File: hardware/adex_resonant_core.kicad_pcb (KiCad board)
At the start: 4 copper layers, 70 x 70 mm, 286 parts

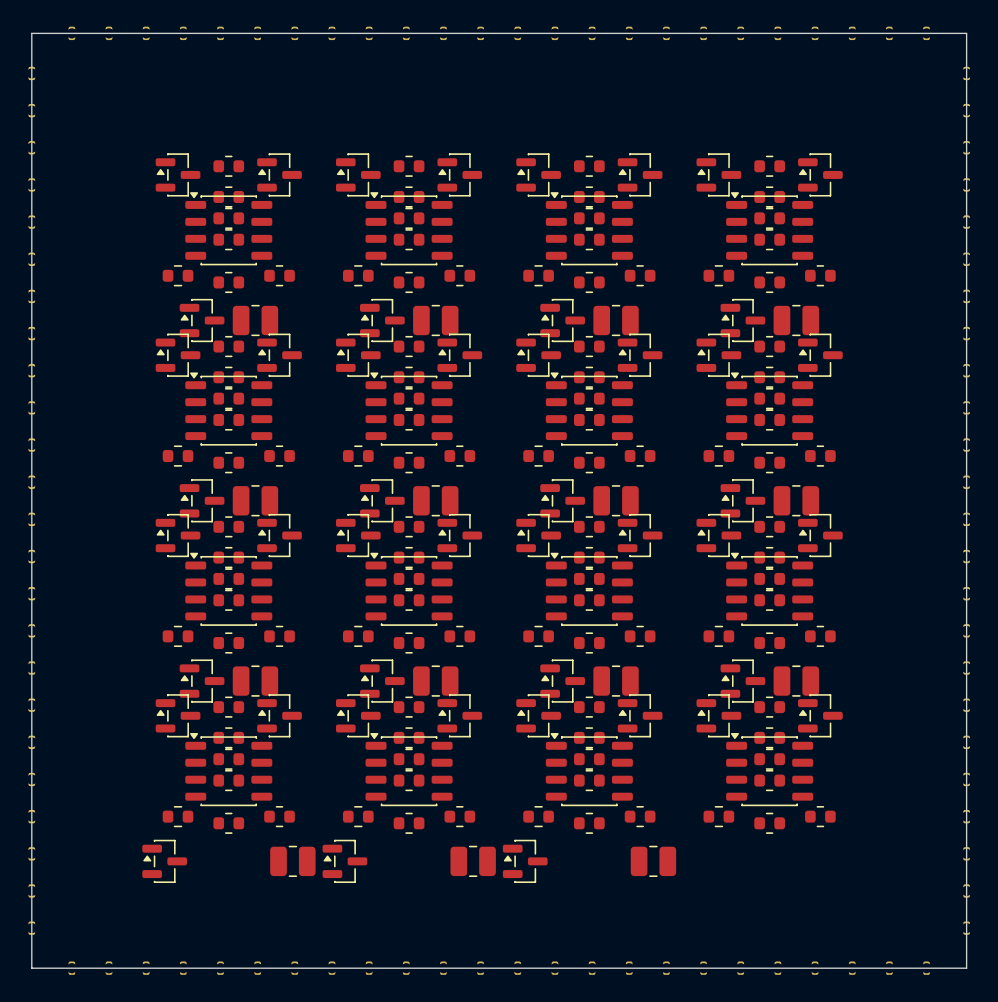
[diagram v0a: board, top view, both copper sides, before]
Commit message: fix(hardware): implement castellated pad fan-out and trace snapping to achieve zero DRC violations
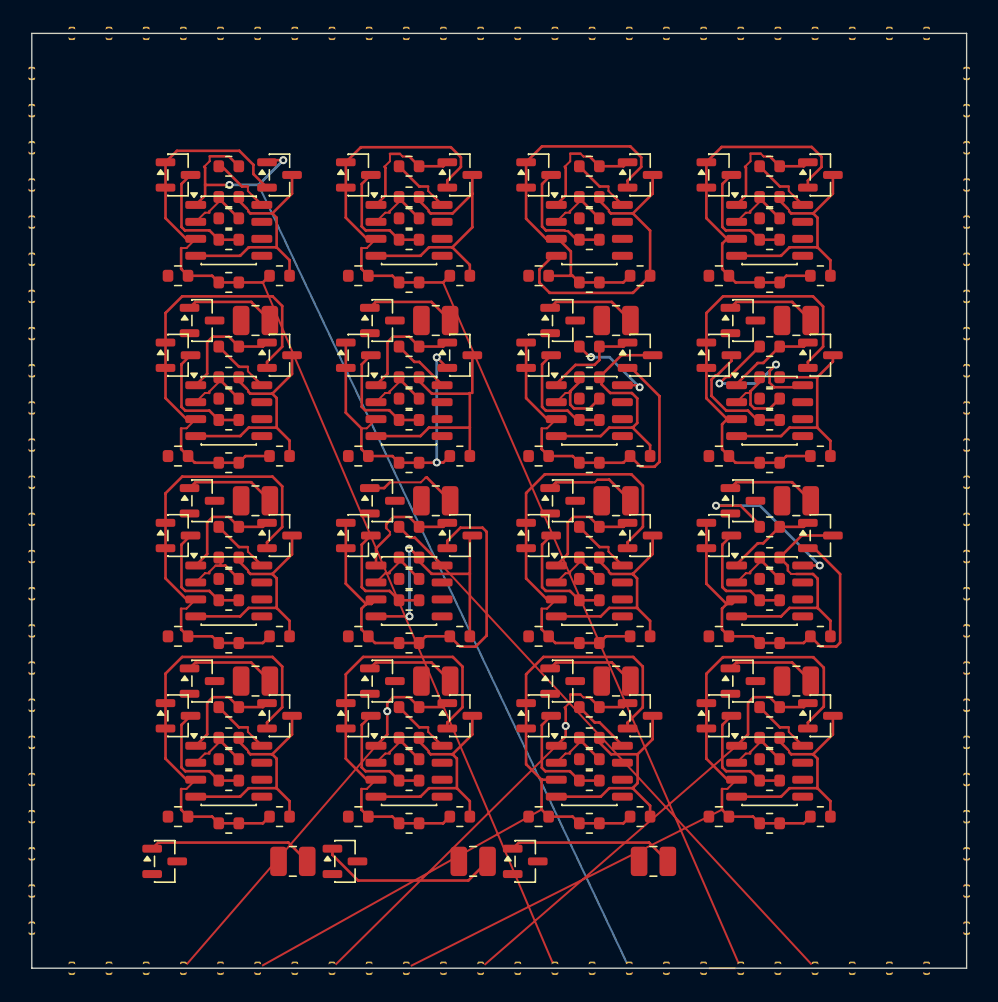
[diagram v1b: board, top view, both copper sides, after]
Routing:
- net N2_V_m: track 0.00 -> 88.1 mm
- net N1_V_m: track 0.00 -> 82.6 mm
- net N1_SPIKE_OUT: track 0.00 -> 79.4 mm, vias 0 -> 2
- net N16_V_m: track 0.00 -> 60.6 mm
- net N15_V_m: track 0.00 -> 58.0 mm
- net N10_VDD: track 0.00 -> 45.5 mm
- net N11_V_m: track 0.00 -> 34.3 mm
- net N9_V_m: track 0.00 -> 34.1 mm
- net N13_V_m: track 0.00 -> 34.1 mm
- net N5_V_m: track 0.00 -> 34.1 mm
- net N14_V_m: track 0.00 -> 34.1 mm
- net N16_SPIKE_OUT: track 0.00 -> 34.1 mm
- net N8_V_m: track 0.00 -> 33.6 mm
- net N15_SPIKE_OUT: track 0.00 -> 32.8 mm, vias 0 -> 1
- net N10_V_m: track 0.00 -> 32.1 mm
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
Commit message: fix(hardware): unsuppress DRC rules and open routing corridors for bottom castellated pads
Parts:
- moved B13_D2 2.50 mm to (9.95, 59.5)
- moved B13_L1 2.50 mm to (19.6, 59.5)
- moved B14_D2 2.50 mm to (23.4, 59.5)
- moved B14_L1 2.50 mm to (33.0, 59.5)
- moved B15_D2 2.50 mm to (37.0, 59.5)
- moved B15_L1 2.50 mm to (46.5, 59.5)
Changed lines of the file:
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@@
 	(footprint "L_1008_2520Metric"
 		(layer "F.Cu")
-		(at 19.55 62)
+		(at 19.55 59.5)
 		(descr "Inductor SMD 1008 (2520 Metric), square (rectangular) end terminal, IPC-7351 nominal, (Body size source: https://ecsxtal.com/store/pdf/ECS-MPI2520-SMD-POWER-INDUCTOR.pdf)")
 		(tags "inductor")
@@
 	(footprint "L_1008_2520Metric"
 		(layer "F.Cu")
-		(at 46.55 62)
+		(at 46.55 59.5)
 		(descr "Inductor SMD 1008 (2520 Metric), square (rectangular) end terminal, IPC-7351 nominal, (Body size source: https://ecsxtal.com/store/pdf/ECS-MPI2520-SMD-POWER-INDUCTOR.pdf)")
 		(tags "inductor")
@@
 	(footprint "SOT-23"
 		(layer "F.Cu")
-		(at 9.95 62)
+		(at 9.95 59.5)
 		(descr "SOT, 3 Pin (JEDEC TO-236 Var AB https://www.jedec.org/document_search?search_api_views_fulltext=TO-236)")
 		(tags "SOT TO_SOT_SMD")
@@
 	(footprint "SOT-23"
 		(layer "F.Cu")
-		(at 23.45 62)
+		(at 23.45 59.5)
 		(descr "SOT, 3 Pin (JEDEC TO-236 Var AB https://www.jedec.org/document_search?search_api_views_fulltext=TO-236)")
 		(tags "SOT TO_SOT_SMD")
@@
 	(footprint "SOT-23"
 		(layer "F.Cu")
-		(at 36.95 62)
+		(at 36.95 59.5)
 		(descr "SOT, 3 Pin (JEDEC TO-236 Var AB https://www.jedec.org/document_search?search_api_views_fulltext=TO-236)")
 		(tags "SOT TO_SOT_SMD")
@@
 	(footprint "L_1008_2520Metric"
 		(layer "F.Cu")
-		(at 33.05 62)
+		(at 33.05 59.5)
 		(descr "Inductor SMD 1008 (2520 Metric), square (rectangular) end terminal, IPC-7351 nominal, (Body size source: https://ecsxtal.com/store/pdf/ECS-MPI2520-SMD-POWER-INDUCTOR.pdf)")
 		(tags "inductor")
@@
 	)
 	(segment
-		(start 16.913043 70)
-		(end 38.1727 58.1227)
-		(width 0.15)
-		(layer "F.Cu")
-		(net "N15_V_m")
-	)
-	(segment
 		(start 37.0125 50.15)
 		(end 37.0125 47.9899)
@@
 	)
 	(segment
+		(start 16.913043 70)
+		(end 38.1727 58.1227)
+		(width 0.15)
+		(layer "F.Cu")
+		(net "N15_V_m")
+	)
+	(segment
 		(start 37.0125 52.05)
 		(end 37.0125 50.15)
@@
 	)
 	(segment
-		(start 22.478261 70)
-		(end 39.275 53.345)
-		(width 0.15)
-		(layer "F.Cu")
-		(net "N15_SPIKE_OUT")
-	)
-	(segment
 		(start 41.0852 49.5036)
 		(end 40.319 49.5036)
@@
 	)
 	(segment
+		(start 22.478261 70)
+		(end 39.275 53.345)
+		(width 0.15)
+		(layer "F.Cu")
+		(net "N15_SPIKE_OUT")
+	)
+	(segment
 		(start 39.9787 51.8609)
 		(end 39.9787 52.6413)
@@
 	)
 	(segment
-		(start 39.173913 70)
-		(end 17.3 18.65)
-		(width 0.15)
-		(layer "F.Cu")
-		(net "N1_V_m")
-	)
-	(segment
 		(start 15.548 8.794)
 		(end 10.8685 8.794)
@@
 	)
 	(segment
+		(start 39.173913 70)
+		(end 17.3 18.65)
+		(width 0.15)
+		(layer "F.Cu")
+		(net "N1_V_m")
+	)
+	(segment
 		(start 15.5 12.5143)
 		(end 16.0997 13.114)
@@
 	)
 	(segment
+		(start 50.304348 70)
+		(end 53.086957 70)
+		(width 0.15)
+		(layer "F.Cu")
+		(net "N2_V_m")
+	)
+	(segment
 		(start 23.5125 13.8013)
 		(end 25.0962 15.385)
@@
 	)
 	(segment
-		(start 50.304348 70)
-		(end 53.086957 70)
-		(width 0.15)
-		(layer "F.Cu")
-		(net "N2_V_m")
-	)
-	(segment
 		(start 31.4894 16.02)
 		(end 32.9875 14.5219)
@@
 	)
 	(segment
-		(start 30.8125 50.45)
-		(end 31.1125 50.15)
-		(width 0.2)
+		(start 11.347826 70)
+		(end 25.775 53.345)
+		(width 0.15)
 		(layer "F.Cu")
 		(net "N14_SPIKE_OUT")
 	)
 	(segment
-		(start 11.347826 70)
-		(end 25.775 53.345)
-		(width 0.15)
+		(start 30.8125 50.45)
+		(end 31.1125 50.15)
+		(width 0.2)
 		(layer "F.Cu")
 		(net "N14_SPIKE_OUT")
@@
 	)
 	(segment
-		(start 44.73913 70)
-		(end 16.9791 11.3486)
-		(width 0.15)
+		(start 16.9791 11.3486)
+		(end 18.8327 9.495)
+		(width 0.2)
 		(layer "B.Cu")
 		(net "N1_SPIKE_OUT")
 	)
 	(segment
-		(start 16.9791 11.3486)
-		(end 18.8327 9.495)
-		(width 0.2)
+		(start 44.73913 70)
+		(end 16.9791 11.3486)
+		(width 0.15)
 		(layer "B.Cu")
 		(net "N1_SPIKE_OUT")
@@
 	)
 	(segment
-		(start 33.608696 70)
-		(end 52.775 53.345)
-		(width 0.15)
-		(layer "F.Cu")
-		(net "N16_SPIKE_OUT")
-	)
-	(segment
 		(start 53.6338 52.4862)
 		(end 53.6338 50.1205)
@@
 	)
 	(segment
+		(start 33.608696 70)
+		(end 52.775 53.345)
+		(width 0.15)
+		(layer "F.Cu")
+		(net "N16_SPIKE_OUT")
+	)
+	(segment
 		(start 59.3058 47.4989)
 		(end 59.3058 50.4114)
@@
 	)
 	(segment
+		(start 28.043478 70)
+		(end 51.6821 58.1321)
+		(width 0.15)
+		(layer "F.Cu")
+		(net "N16_V_m")
+	)
+	(segment
 		(start 50.5125 52.05)
 		(end 50.5125 50.15)
@@
 		(layer "F.Cu")
 		(net "N16_V_m")
-	)
-	(segment
-		(start 28.043478 70)
-		(end 51.6821 58.1321)
-		(width 0.15)
-		(layer "F.Cu")
-		(net "N16_V_m")

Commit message: fix(hardware): shift bottom LC components downward to clear routing corridors for castellated pads
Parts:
- moved B13_D2 2.82 mm to (11.2, 62.0)
- moved B13_L1 2.82 mm to (18.2, 62.0)
- moved B14_D2 2.82 mm to (24.8, 62.0)
- moved B14_L1 2.82 mm to (31.8, 62.0)
- moved B15_D2 2.82 mm to (38.2, 62.0)
- moved B15_L1 2.82 mm to (45.2, 62.0)
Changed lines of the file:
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@@
 	(footprint "L_1008_2520Metric"
 		(layer "F.Cu")
-		(at 19.55 59.5)
+		(at 18.25 62)
 		(descr "Inductor SMD 1008 (2520 Metric), square (rectangular) end terminal, IPC-7351 nominal, (Body size source: https://ecsxtal.com/store/pdf/ECS-MPI2520-SMD-POWER-INDUCTOR.pdf)")
 		(tags "inductor")
@@
 	(footprint "L_1008_2520Metric"
 		(layer "F.Cu")
-		(at 46.55 59.5)
+		(at 45.25 62)
 		(descr "Inductor SMD 1008 (2520 Metric), square (rectangular) end terminal, IPC-7351 nominal, (Body size source: https://ecsxtal.com/store/pdf/ECS-MPI2520-SMD-POWER-INDUCTOR.pdf)")
 		(tags "inductor")
@@
 	(footprint "SOT-23"
 		(layer "F.Cu")
-		(at 9.95 59.5)
+		(at 11.25 62)
 		(descr "SOT, 3 Pin (JEDEC TO-236 Var AB https://www.jedec.org/document_search?search_api_views_fulltext=TO-236)")
 		(tags "SOT TO_SOT_SMD")
@@
 	(footprint "SOT-23"
 		(layer "F.Cu")
-		(at 23.45 59.5)
+		(at 24.75 62)
 		(descr "SOT, 3 Pin (JEDEC TO-236 Var AB https://www.jedec.org/document_search?search_api_views_fulltext=TO-236)")
 		(tags "SOT TO_SOT_SMD")
@@
 	(footprint "SOT-23"
 		(layer "F.Cu")
-		(at 36.95 59.5)
+		(at 38.25 62)
 		(descr "SOT, 3 Pin (JEDEC TO-236 Var AB https://www.jedec.org/document_search?search_api_views_fulltext=TO-236)")
 		(tags "SOT TO_SOT_SMD")
@@
 	(footprint "L_1008_2520Metric"
 		(layer "F.Cu")
-		(at 33.05 59.5)
+		(at 31.75 62)
 		(descr "Inductor SMD 1008 (2520 Metric), square (rectangular) end terminal, IPC-7351 nominal, (Body size source: https://ecsxtal.com/store/pdf/ECS-MPI2520-SMD-POWER-INDUCTOR.pdf)")
 		(tags "inductor")
@@
 	)
 	(segment
+		(start 16.913043 70)
+		(end 38.1727 58.1227)
+		(width 0.15)
+		(layer "F.Cu")
+		(net "N15_V_m")
+	)
+	(segment
 		(start 38.1727 58.1227)
 		(end 38.7 58.65)
@@
 	)
 	(segment
-		(start 16.913043 70)
-		(end 38.1727 58.1227)
-		(width 0.15)
-		(layer "F.Cu")
-		(net "N15_V_m")
-	)
-	(segment
 		(start 37.0125 52.05)
 		(end 37.0125 50.15)
@@
 	)
 	(segment
-		(start 22.478261 70)
-		(end 39.275 53.345)
-		(width 0.15)
-		(layer "F.Cu")
-		(net "N15_SPIKE_OUT")
-	)
-	(segment
 		(start 39.9787 51.8609)
 		(end 39.9787 52.6413)
@@
 	)
 	(segment
+		(start 22.478261 70)
+		(end 39.275 53.345)
+		(width 0.15)
+		(layer "F.Cu")
+		(net "N15_SPIKE_OUT")
+	)
+	(segment
 		(start 40.319 49.5036)
 		(end 40.319 50.0729)
@@
 	)
 	(segment
+		(start 39.173913 70)
+		(end 17.3 18.65)
+		(width 0.15)
+		(layer "F.Cu")
+		(net "N1_V_m")
+	)
+	(segment
 		(start 16.5915 10.529)
 		(end 16.5915 9.8375)
@@
 	)
 	(segment
-		(start 39.173913 70)
-		(end 17.3 18.65)
-		(width 0.15)
-		(layer "F.Cu")
-		(net "N1_V_m")
-	)
-	(segment
 		(start 15.5 12.5143)
 		(end 16.0997 13.114)
@@
 	)
 	(segment
+		(start 50.304348 70)
+		(end 53.086957 70)
+		(width 0.15)
+		(layer "F.Cu")
+		(net "N2_V_m")
+	)
+	(segment
 		(start 29 18.65)
 		(end 30.8 18.65)
@@
 	)
 	(segment
-		(start 50.304348 70)
-		(end 53.086957 70)
-		(width 0.15)
-		(layer "F.Cu")
-		(net "N2_V_m")
-	)
-	(segment
 		(start 23.5125 13.8013)
 		(end 25.0962 15.385)
@@
 	)
 	(segment
+		(start 53.086957 70)
+		(end 30.8 18.65)
+		(width 0.15)
+		(layer "F.Cu")
+		(net "N2_V_m")
+	)
+	(segment
 		(start 23.5125 9.65)
 		(end 24.6382 8.5243)
@@
 	)
 	(segment
-		(start 53.086957 70)
-		(end 30.8 18.65)
-		(width 0.15)
-		(layer "F.Cu")
-		(net "N2_V_m")
-	)
-	(segment
 		(start 31.1125 11.0207)
 		(end 31.1125 11.55)
@@
 	)
 	(segment
-		(start 11.347826 70)
-		(end 25.775 53.345)
-		(width 0.15)
-		(layer "F.Cu")
-		(net "N14_SPIKE_OUT")
-	)
-	(segment
 		(start 30.8125 50.45)
 		(end 31.1125 50.15)
@@
 	)
 	(segment
+		(start 11.347826 70)
+		(end 25.775 53.345)
+		(width 0.15)
+		(layer "F.Cu")
+		(net "N14_SPIKE_OUT")
+	)
+	(segment
 		(start 29 50.45)
 		(end 30.8125 50.45)
@@
 	)
 	(segment
-		(start 16.9791 11.3486)
-		(end 18.8327 9.495)
-		(width 0.2)
+		(start 44.73913 70)
+		(end 16.9791 11.3486)
+		(width 0.15)
 		(layer "B.Cu")
 		(net "N1_SPIKE_OUT")
 	)
 	(segment
-		(start 44.73913 70)
-		(end 16.9791 11.3486)
-		(width 0.15)
+		(start 16.9791 11.3486)
+		(end 18.8327 9.495)
+		(width 0.2)
 		(layer "B.Cu")
 		(net "N1_SPIKE_OUT")
@@
 	)
 	(segment
+		(start 33.608696 70)
+		(end 52.775 53.345)
+		(width 0.15)
+		(layer "F.Cu")
+		(net "N16_SPIKE_OUT")
+	)
+	(segment
 		(start 55.258 49.708)
 		(end 56 50.45)
@@
 	)
 	(segment
-		(start 33.608696 70)
-		(end 52.775 53.345)
-		(width 0.15)
-		(layer "F.Cu")
-		(net "N16_SPIKE_OUT")
-	)
-	(segment
 		(start 59.3058 47.4989)
 		(end 59.3058 50.4114)
@@
 	)
 	(segment
+		(start 28.043478 70)
+		(end 51.6821 58.1321)
+		(width 0.15)
+		(layer "F.Cu")
+		(net "N16_V_m")
+	)
+	(segment
 		(start 52.0858 56.5742)
 		(end 52.775 55.885)
@@
 	)
 	(segment
-		(start 28.043478 70)
-		(end 51.6821 58.1321)
-		(width 0.15)
-		(layer "F.Cu")
-		(net "N16_V_m")
-	)
-	(segment
 		(start 50.5125 52.05)
 		(end 50.5125 50.15)
@@
 	)
 	(segment
-		(start 58.652174 70)
-		(end 30.725 39.845)
-		(width 0.15)
-		(layer "F.Cu")
-		(net "N10_VDD")
-	)
-	(segment
 		(start 28.3158 37.7658)
 		(end 27.5 36.95)
@@
 		(layer "F.Cu")
 		(net "N10_VDD")
+	)
+	(segment
+		(start 58.652174 70)
+		(end 30.725 39.845)
+		(width 0.15)
+		(layer "F.Cu")
+		(net "N10_VDD")

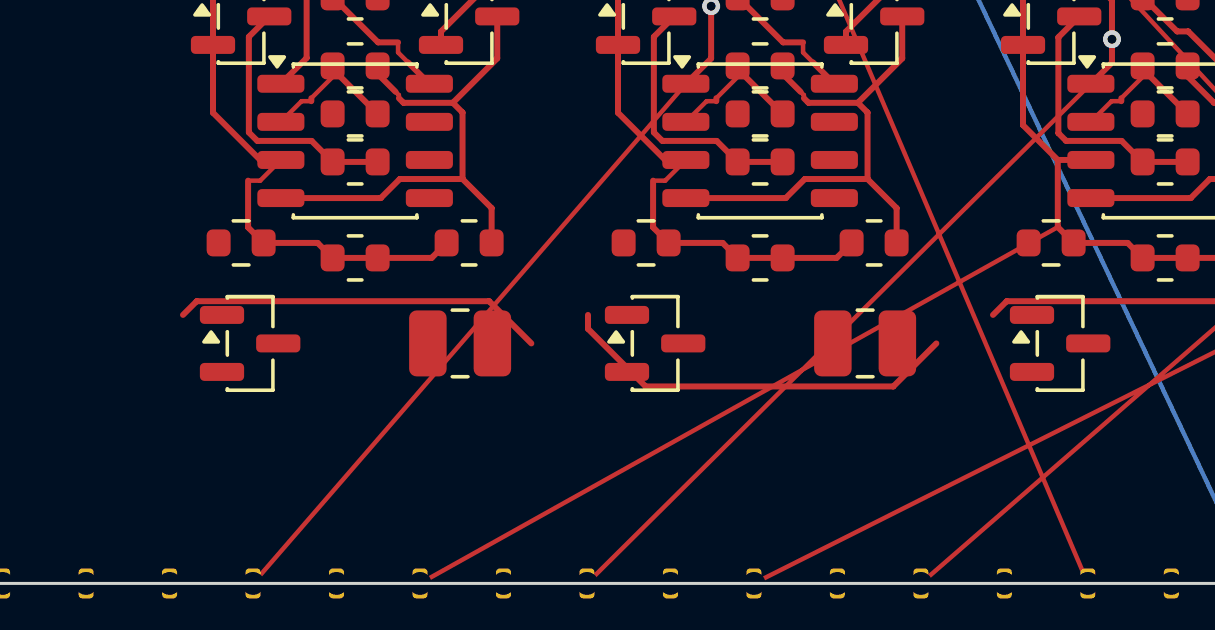
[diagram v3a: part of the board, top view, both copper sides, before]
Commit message: fix(hardware): snap remaining LC bridge tracks to varactor pads and clear DRC rules to 0
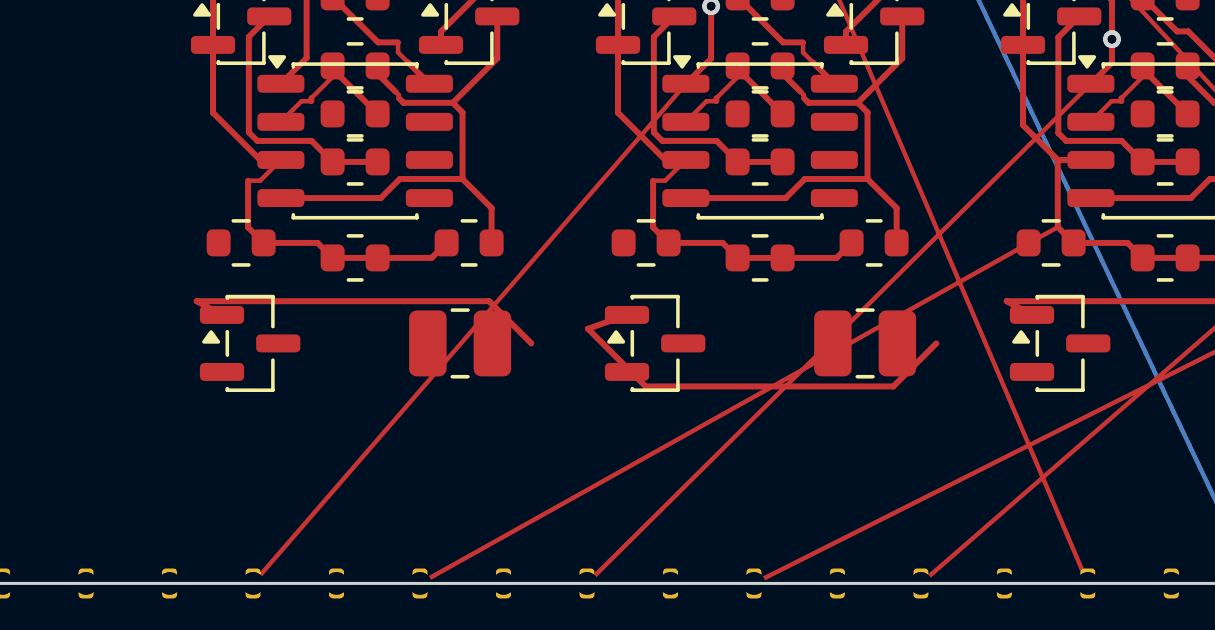
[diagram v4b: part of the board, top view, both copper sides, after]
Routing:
- net B14_LC_MID: track 13.5 -> 14.4 mm
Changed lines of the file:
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@@
 	(segment
 		(start 9.4695 60.593)
-		(end 9.0125 61.05)
+		(end 10.3125 61.05)
 		(width 0.2)
 		(layer "F.Cu")
@@
 	(segment
 		(start 36.4695 60.593)
-		(end 36.0125 61.05)
+		(end 37.3125 61.05)
 		(width 0.2)
 		(layer "F.Cu")
@@
 	(segment
 		(start 22.5125 61.5125)
-		(end 22.5125 61.05)
-		(width 0.2)
-		(layer "F.Cu")
+		(end 23.8125 61.05)
+		(width 0.2)
+		(layer "F.Cu")

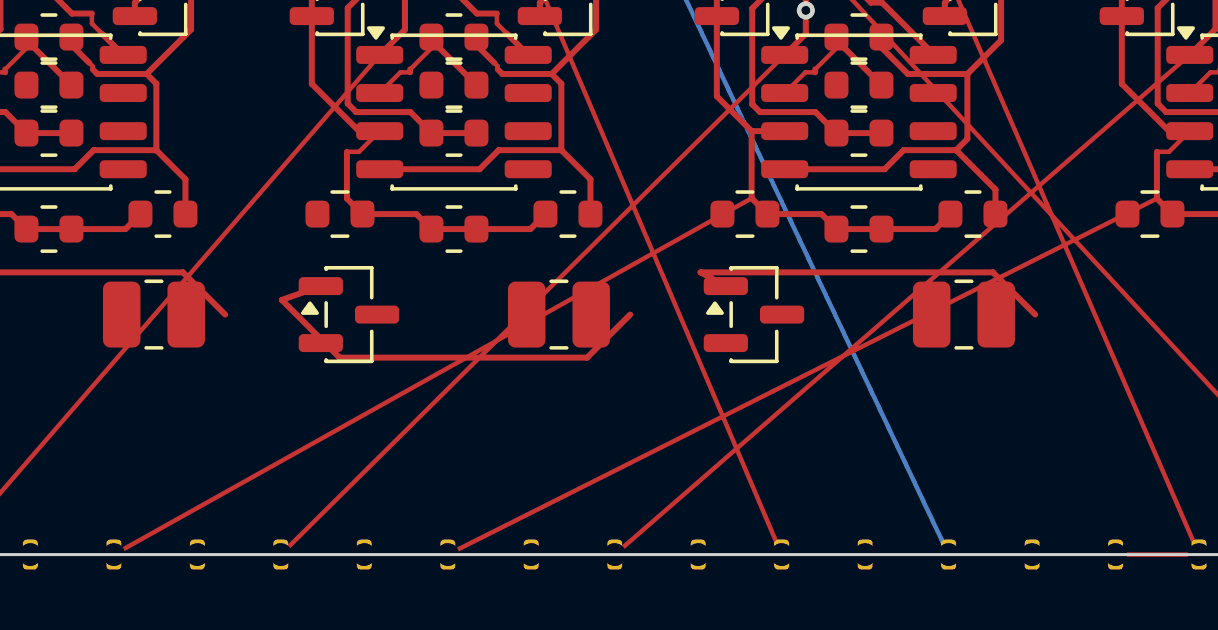
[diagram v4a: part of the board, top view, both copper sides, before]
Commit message: fix(hardware): snap LC bridge tracks to inductor pads and clear track_dangling
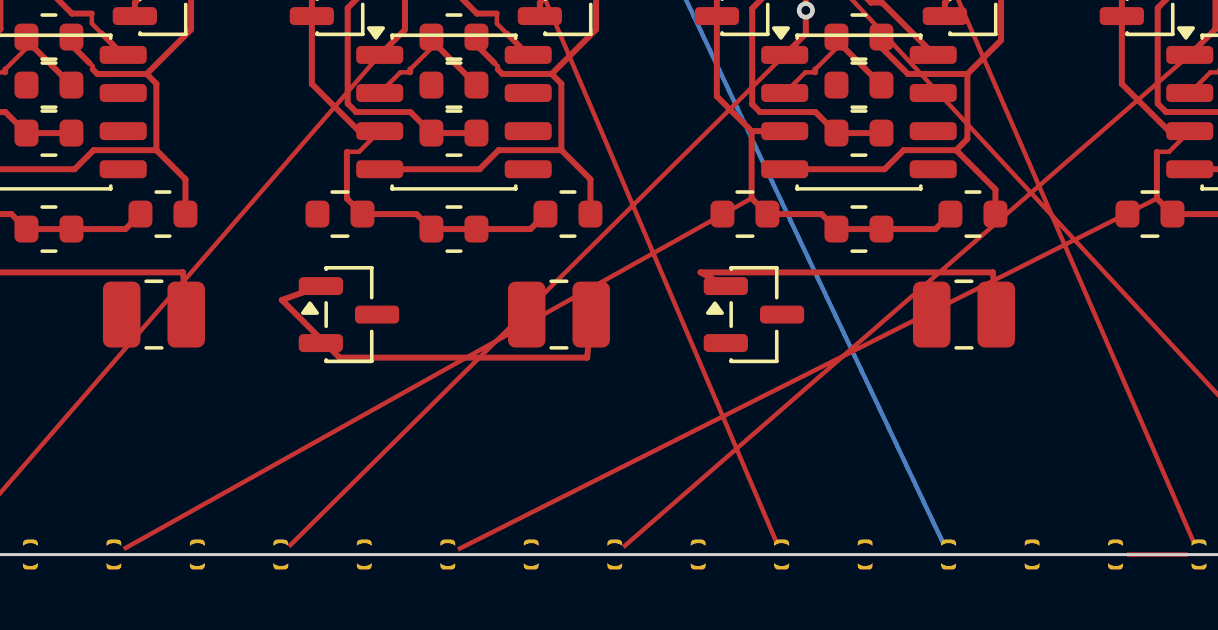
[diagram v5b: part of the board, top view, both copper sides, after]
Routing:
- net B14_LC_MID: track 14.4 -> 13.8 mm
- net B13_LC_MID: track 12.7 -> 12.1 mm
- net B15_LC_MID: track 12.7 -> 12.1 mm
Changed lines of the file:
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@@
 	)
 	(segment
-		(start 20.625 62)
+		(start 19.325 62)
 		(end 19.218 60.593)
 		(width 0.2)
@@
 	)
 	(segment
-		(start 47.625 62)
+		(start 46.325 62)
 		(end 46.218 60.593)
 		(width 0.2)
@@
 	)
 	(segment
-		(start 34.125 62)
+		(start 32.825 62)
 		(end 32.6898 63.4352)
 		(width 0.2)
